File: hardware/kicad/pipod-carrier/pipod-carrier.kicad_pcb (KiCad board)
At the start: 2 copper layers, 65 x 105 mm, 22 parts, among them J1 Raspberry_Pi_Zero_2W, J3 Conn_02x06_Odd_Even, J5 Conn_01x02, SW1 Volume Up, SW2 Volume Down, U1 Adafruit Seesaw Encoder, U3 PCM5102A, U4 TPA6132

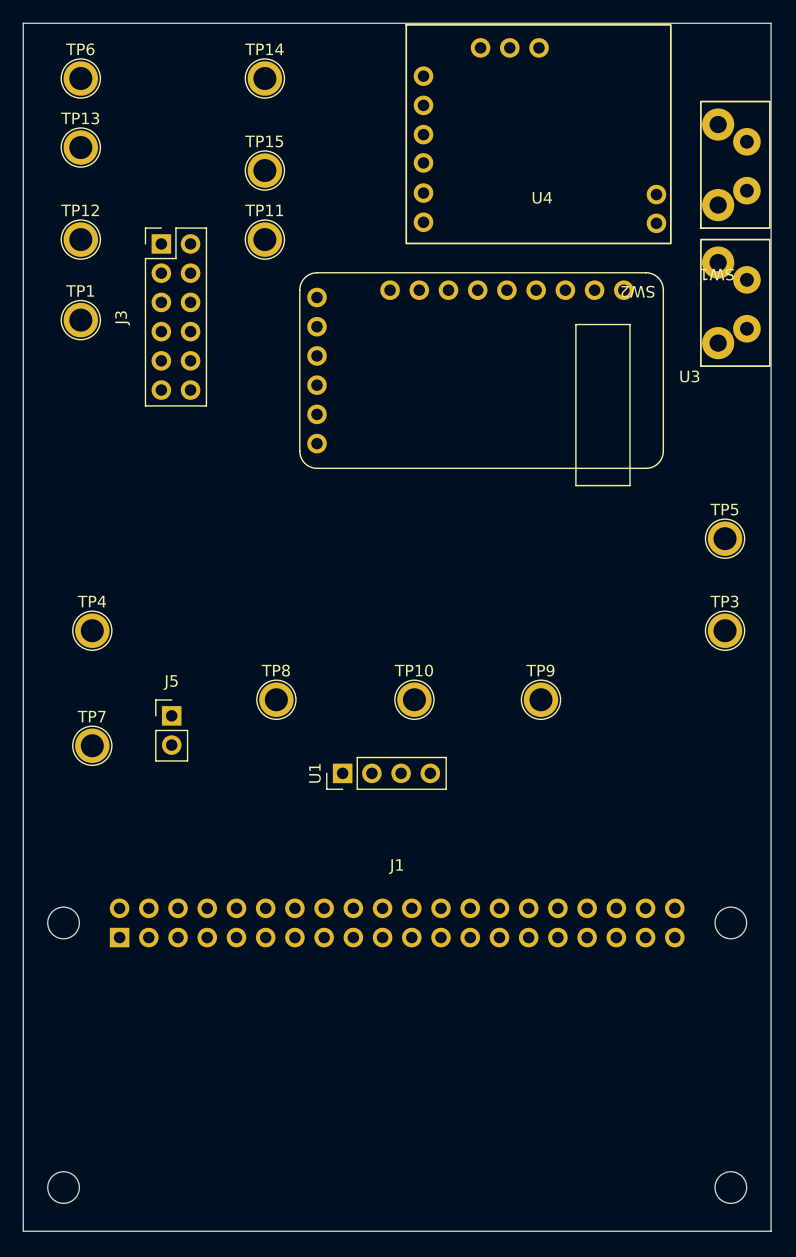
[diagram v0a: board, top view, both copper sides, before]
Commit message: Initial PCB layout complete
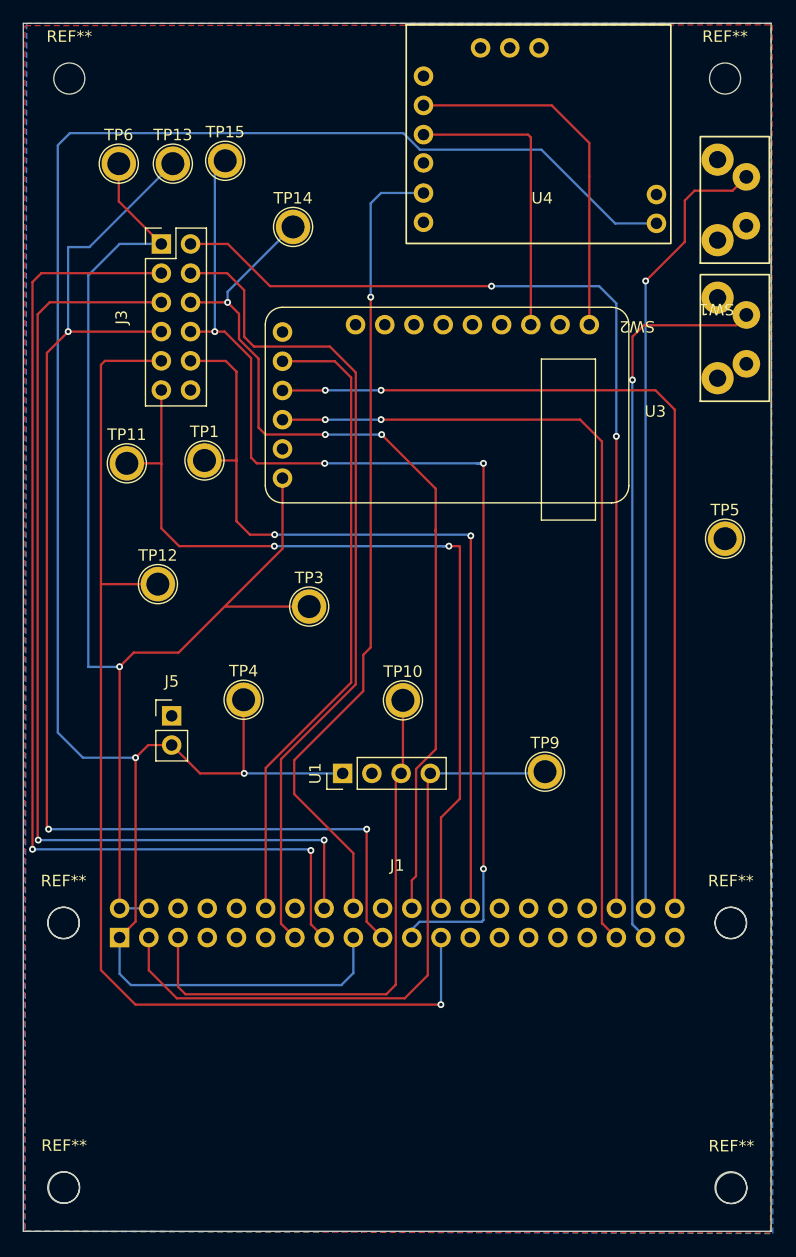
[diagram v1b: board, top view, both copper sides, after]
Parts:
- removed TP7: TP_TFT_3V3, TestPoint:TestPoint_Plated_Hole_D2.0mm
- removed TP8: TP_SEESAW_3V3, TestPoint:TestPoint_Plated_Hole_D2.0mm
- added REF**: MountingHole_2.7mm_M2.5, MountingHole:MountingHole_2.7mm_M2.5, F.Cu at (103.5, 118.4)
- added REF**: MountingHole_2.7mm_M2.5, MountingHole:MountingHole_2.7mm_M2.5, F.Cu at (161.5, 118.4)
- added REF**: MountingHole_2.7mm_M2.5, MountingHole:MountingHole_2.7mm_M2.5, F.Cu at (103.5, 141.4)
- added REF**: MountingHole_2.7mm_M2.5, MountingHole:MountingHole_2.7mm_M2.5, F.Cu at (161.6, 141.4)
- added REF**: MountingHole_2.7mm_M2.5, MountingHole:MountingHole_2.7mm_M2.5, F.Cu at (104.0, 45.0)
- added REF**: MountingHole_2.7mm_M2.5, MountingHole:MountingHole_2.7mm_M2.5, F.Cu at (161.0, 45.0)
- moved TP3 36.2 mm to (124.8, 90.9)
- moved TP12 30.7 mm to (111.7, 89.0)
- moved TP11 22.9 mm to (109.0, 78.5)
- moved TP1 16.3 mm to (115.8, 78.2)
- moved TP4 14.5 mm to (119.2, 99.0)
- moved TP14 13.1 mm to (123.5, 57.9)
- moved TP13 8.12 mm to (113.0, 52.4)
- moved TP6 8.10 mm to (108.3, 52.4)
- moved TP9 6.26 mm to (145.3, 105.2)
- moved U3 4.24 mm to (136.8, 73.4)
- moved TP15 3.55 mm to (117.5, 52.1)
- moved SW1 3.05 mm to (160.3, 55.5)
- moved SW2 3.05 mm to (160.3, 67.5)
- moved TP10 1.00 mm to (133.0, 99.0)
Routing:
- net /3V3: track 0.00 -> 183.9 mm, vias 0 -> 2
- net /TFT_MOSI: track 0.00 -> 109.0 mm, vias 0 -> 3
- net /5V: track 0.00 -> 108.3 mm, vias 0 -> 1
- net /TFT_SCLK: track 0.00 -> 99.6 mm, vias 0 -> 1
- net /TFT_MISO: track 0.00 -> 99.2 mm, vias 0 -> 4
- net /TFT_BTN4: track 0.00 -> 93.3 mm, vias 0 -> 2
- net /TFT_BTN1: track 0.00 -> 92.0 mm, vias 0 -> 2
- net /TFT_BTN3: track 0.00 -> 87.6 mm, vias 0 -> 2
- net /TFT_DC: track 0.00 -> 79.9 mm, vias 0 -> 3
- net Net-(J1-GPIO21_/_DIN): track 0.00 -> 78.2 mm, vias 0 -> 2
- net /TFT_CE1: track 0.00 -> 75.5 mm, vias 0 -> 2
- net /TFT_CE0: track 0.00 -> 73.8 mm, vias 0 -> 2
- net /TFT_BTN2: track 0.00 -> 72.6 mm
- net Net-(J1-GPIO19_/_LRCLK): track 0.00 -> 72.4 mm, vias 0 -> 2
- net Net-(J1-GPIO24): track 0.00 -> 71.1 mm, vias 0 -> 1
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- added copper zone on B.Cu, net GND
- added copper zone on F.Cu, net GND

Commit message: PCB first draft with no errors and updated component placement
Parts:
- removed the REF** at (103.5, 118.4)
- removed the REF** at (161.5, 118.4)
- removed the REF** at (103.5, 141.4)
- removed the REF** at (161.6, 141.4)
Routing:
- net GND: track 0.00 -> 6.13 mm
